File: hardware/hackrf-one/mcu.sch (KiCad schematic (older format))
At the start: 132 parts, among them J1 GSG-USB-MICRO-B, P1 1V8, P10 CTOUT_2, P11 CTIN_2, P12 U3_RXD, P13 U3_TXD, P19 SPIFI, P20 GPIO, P21 ANALOG, P22 I2S, P23 DBGEN, P24 TRST, P25 LPC_ISP, P26 LPC_JTAG, P27 CONN_3, P28 SD, P29 CPLD_JTAG, P3 GND, P30 BANK2_AUX, P31 BANK1_AUX, P32 CONN_3, P33 CONN_3, P34 CONN_3, P35 GCK0, P5 WAKEUP, P6 TRACECLK, P7 CTIN_4, P8 VCC, P9 CTOUT_4, U20 W25Q80BV, U21 TPS62410, U22 GSG-IP4220CZ6, U23 LPC43XXFBD144, U24 GSG-XC2C64A-7VQG100C, X2 MCU_XTAL

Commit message: removed boot headers, added reset and DFU pushbuttons
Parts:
- removed P27, P32, P33, P34: CONN_3, symbol CONN_3
- removed R40, R42, R43, R82: 10k, symbol R
- added SW1: DFU, symbol SW_PUSH
- added SW2: RESET, symbol SW_PUSH
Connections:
- wire segments 529 -> 590
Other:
- note added: "Default boot configuration is SPIFI.\nPress SW1 during reset to switch to\nUSB0 (DFU mode)."
- note removed: "Default boot configuration is SPIFI.\nInstall headers and jumpers (and\noptionally resistors) to reconfigure."
- moved on the sheet: R67, R68, R7, R93

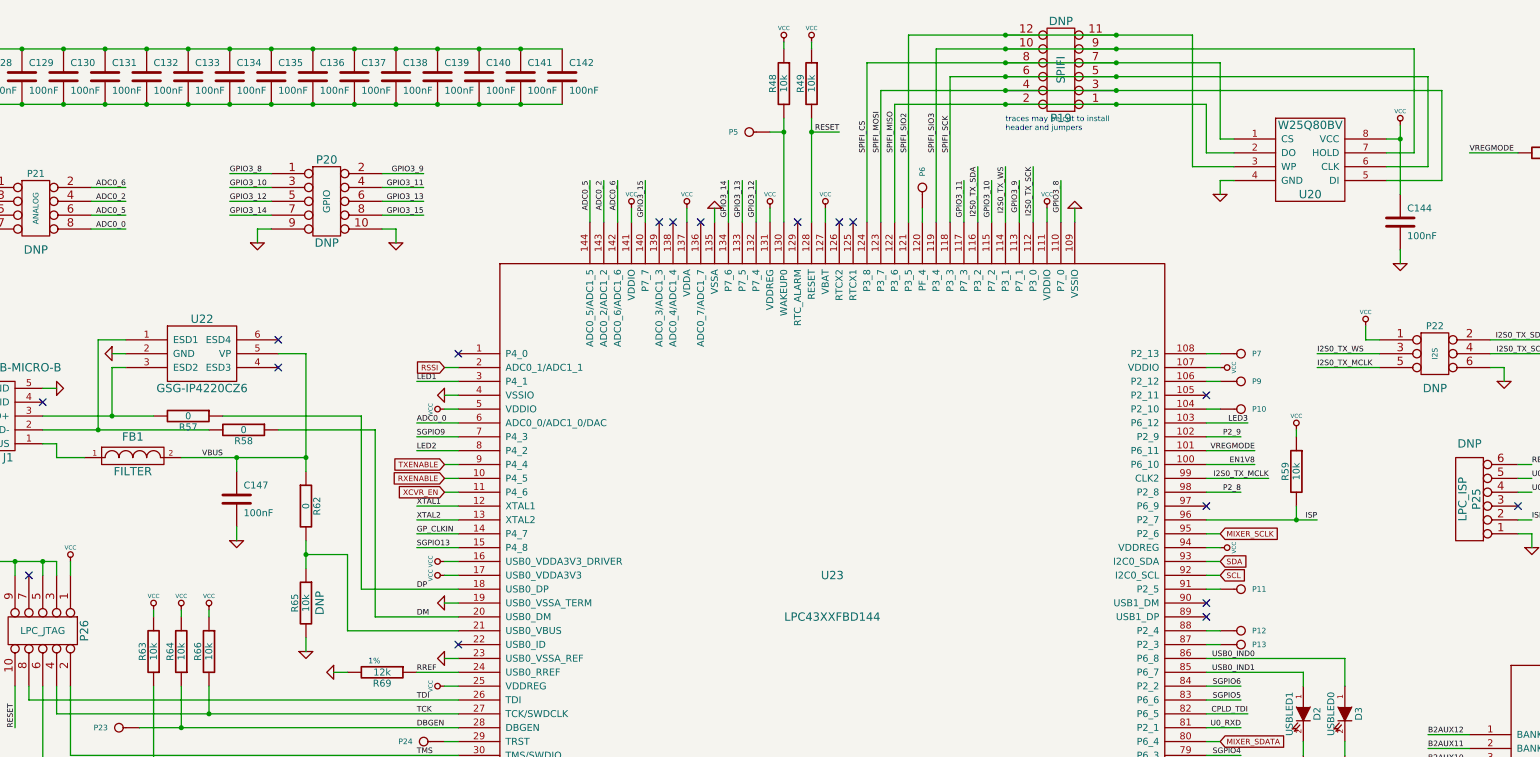
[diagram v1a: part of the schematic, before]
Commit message: removed some DNP parts and 0 ohm resistors
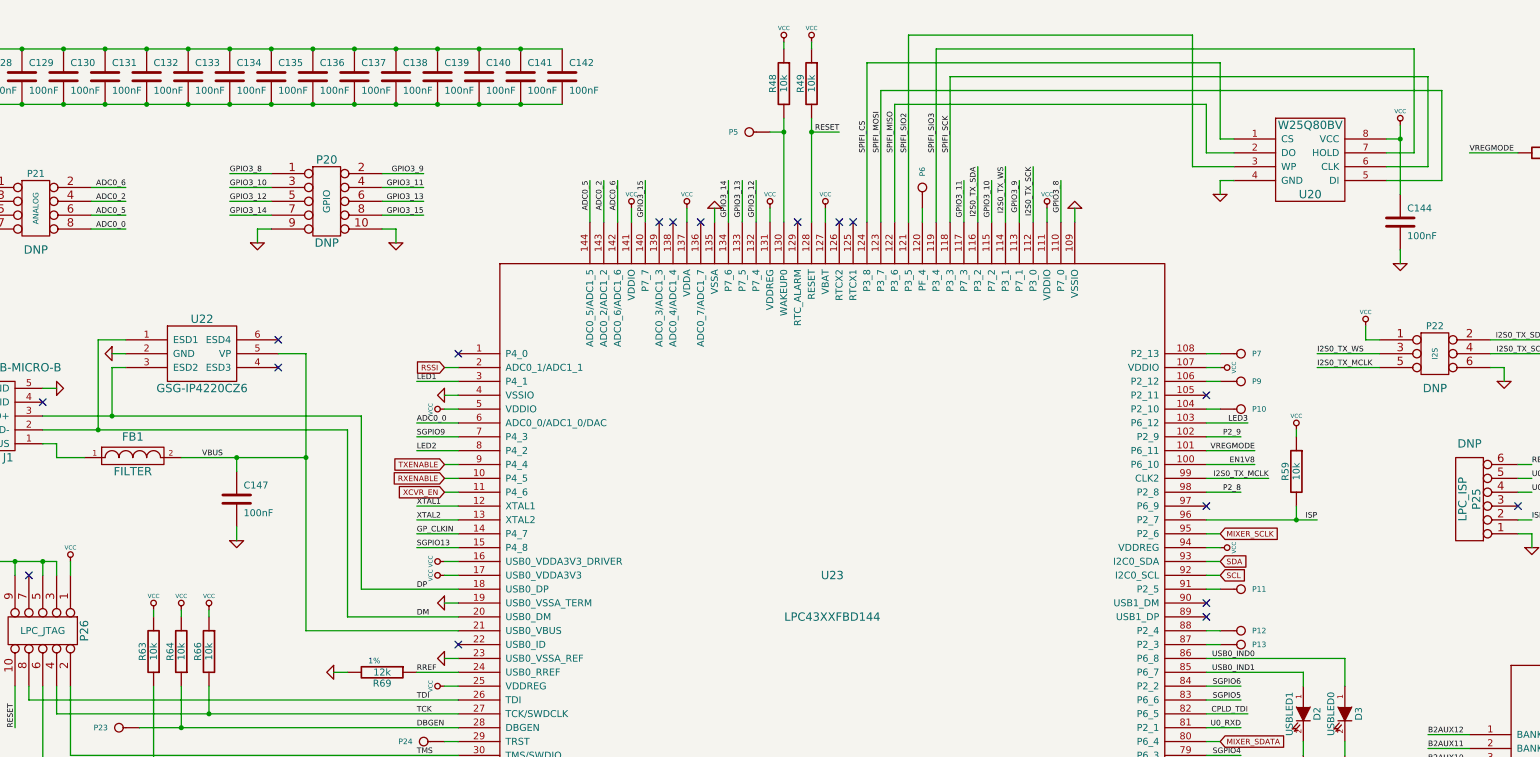
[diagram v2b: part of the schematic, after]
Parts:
- removed P19: SPIFI, symbol CONN_6X2
- removed R57, R58, R62: 0, symbol R
- removed R65: 10k, symbol R
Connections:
- net DM: now also J1.2 (D-), U22.1 (ESD1)
- net DP: now also J1.3 (D+), U22.3 (ESD2)
- net VBUS: now also U23.21 (USB0_VBUS)
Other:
- note removed: "traces may be cut to install\nheader and jumpers"
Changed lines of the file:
@@
 Wire Wire Line
 	11450 10000 11850 10000
-Connection ~ 8250 700
-Connection ~ 9050 700
 Wire Wire Line
-	7550 700  8250 700
+	7550 700  9600 700
 Wire Wire Line
-	8250 700  9050 700
-Wire Wire Line
-	9050 700  9600 700
-Connection ~ 8250 900
-Connection ~ 9050 900
-Wire Wire Line
-	7250 900  8250 900
-Wire Wire Line
-	8250 900  9050 900
-Wire Wire Line
-	9050 900  9800 900
-Connection ~ 8250 1100
-Connection ~ 9050 1100
-Wire Wire Line
-	7350 1100 8250 1100
-Wire Wire Line
-	8250 1100 9050 1100
-Wire Wire Line
-	9050 1100 11400 1100
+	7250 900  9800 900
 Wire Wire Line
 	12650 4400 12950 4400
@@
 	10400 5800 10400 5900
 Wire Wire Line
-	3000 3550 3700 3550
-Wire Wire Line
-	2600 3450 3600 3450
-Wire Wire Line
-	3200 4450 3500 4450
-Wire Wire Line
-	4300 3200 4000 3200
+	1300 3550 1700 3550
 Wire Wire Line
-	4300 5000 3500 5000
+	1700 3550 3500 3550
 Wire Wire Line
-	3500 5000 3500 4450
-Connection ~ 3200 4450
+	1300 3450 1800 3450
 Wire Wire Line
-	3200 4350 3200 4450
+	1800 3450 3600 3450
 Wire Wire Line
-	3200 4450 3200 4550
+	4300 3200 4000 3200
 Wire Wire Line
 	1900 7050 1900 7150
@@
 	1800 3000 1900 3000
 Wire Wire Line
-	3700 3550 3700 4900
+	3500 3550 3500 4900
 Connection ~ 750  2100
 Wire Wire Line
@@
 	5650 2050 5650 1750
 Wire Wire Line
-	3700 4900 4300 4900
+	3500 4900 4300 4900
 Wire Wire Line
 	2700 4350 2700 4250
@@
 	1600 7050 1600 7150
 Wire Wire Line
-	3200 5150 3200 5050
-Wire Wire Line
-	3200 3000 3200 3750
-Wire Wire Line
-	3200 3750 3200 3850
-Wire Wire Line
 	4300 3700 4000 3700
 Wire Wire Line
-	1300 3450 1800 3450
-Wire Wire Line
-	1800 3450 2100 3450
-Wire Wire Line
-	1300 3550 1700 3550
-Wire Wire Line
-	1700 3550 2500 3550
-Wire Wire Line
 	10400 5300 10400 5400
 Wire Wire Line
@@
 	5000 10250 5000 10150
 Wire Wire Line
-	7450 1200 8250 1200
-Wire Wire Line
-	8250 1200 9050 1200
-Wire Wire Line
-	9050 1200 9700 1200
-Connection ~ 9050 1200
-Connection ~ 8250 1200
-Wire Wire Line
-	7850 1000 8250 1000
-Wire Wire Line
-	8250 1000 9050 1000
+	7850 1000 11300 1000
 Wire Wire Line
-	9050 1000 11300 1000
-Connection ~ 9050 1000
-Connection ~ 8250 1000
-Wire Wire Line
-	7750 800  8250 800
-Wire Wire Line
-	8250 800  9050 800
-Wire Wire Line
-	9050 800  11200 800
-Connection ~ 9050 800
-Connection ~ 8250 800
+	7750 800  11200 800
 Wire Wire Line
 	10950 10000 10650 10000
@@
 C155 and C156 values\nare a guess. The datasheet\ndoesn't state the acceptable\nvoltage range for GP_CLKIN.
 $Comp
-L R R65
-U 1 1 506B55A7
-P 3200 4800
-F 0 "R65" V 3280 4800 50  0000 C CNN
-F 1 "10k" V 3200 4800 50  0000 C CNN
-F 2 "" H 3200 4800 60  0001 C CNN
-F 3 "" H 3200 4800 60  0001 C CNN
-F 4 "Stackpole" H 3200 4800 60  0001 C CNN "Manufacturer"
-F 5 "RMCF0402JT10K0" H 3200 4800 60  0001 C CNN "Part Number"
-F 6 "RES 10K OHM 1/16W 5% 0402 SMD" H 3200 4800 60  0001 C CNN "Description"
-F 7 "DNP" V 3100 4800 60  0000 C CNN "Note"
-	1    3200 4800
-	-1   0    0    -1
-$EndComp
-$Comp
-L R R62
-U 1 1 506B54E9
-P 3200 4100
-F 0 "R62" V 3280 4100 50  0000 C CNN
-F 1 "0" V 3200 4100 50  0000 C CNN
-F 2 "" H 3200 4100 60  0001 C CNN
-F 3 "" H 3200 4100 60  0001 C CNN
-F 4 "Stackpole" H 3200 4100 60  0001 C CNN "Manufacturer"
-F 5 "RMCF0402ZT0R00" H 3200 4100 60  0001 C CNN "Part Number"
-F 6 "RES 0.0 OHM 1/16W 0402 SMD" H 3200 4100 60  0001 C CNN "Description"
-	1    3200 4100
-	1    0    0    -1
-$EndComp
-$Comp
 L C C125
 U 1 1 505E9E4C
@@
 Text Notes 2200 9200 0    40   ~ 0
 Default boot configuration is SPIFI.\nPress SW1 during reset to switch to\nUSB0 (DFU mode).
-Text Notes 8250 1400 0    40   ~ 0
-traces may be cut to install\nheader and jumpers
 Text Notes 12000 9550 0    40   ~ 0
 R97 may be installed to connect SGPIO8 to the CPLD.\nBy default SGPIO8 is used as a clock input.
@@
 P2_8
 $Comp
-L R R58
-U 1 1 503F9D27
-P 2750 3550
-F 0 "R58" V 2830 3550 50  0000 C CNN
-F 1 "0" V 2750 3550 50  0000 C CNN
-F 2 "" H 2750 3550 60  0001 C CNN
-F 3 "" H 2750 3550 60  0001 C CNN
-F 4 "Stackpole" H 2750 3550 60  0001 C CNN "Manufacturer"
-F 5 "RMCF0402ZT0R00" H 2750 3550 60  0001 C CNN "Part Number"
-F 6 "RES 0.0 OHM 1/16W 0402 SMD" H 2750 3550 60  0001 C CNN "Description"
-	1    2750 3550
-	0    1    1    0
-$EndComp
-$Comp
-L R R57
-U 1 1 503F9D26
-P 2350 3450
-F 0 "R57" V 2430 3450 50  0000 C CNN
-F 1 "0" V 2350 3450 50  0000 C CNN
-F 2 "" H 2350 3450 60  0001 C CNN
-F 3 "" H 2350 3450 60  0001 C CNN
-F 4 "Stackpole" H 2350 3450 60  0001 C CNN "Manufacturer"
-F 5 "RMCF0402ZT0R00" H 2350 3450 60  0001 C CNN "Part Number"
-F 6 "RES 0.0 OHM 1/16W 0402 SMD" H 2350 3450 60  0001 C CNN "Description"
-	1    2350 3450
-	0    1    1    0
-$EndComp
-$Comp
 L R R59
 U 1 1 503F9A36
@@
 Text Label 4000 3200 0    40   ~ 0
 LED1
-$Comp
-L GND #PWR245
-U 1 1 4F83C49F
-P 3200 5150
-F 0 "#PWR245" H 3200 5150 30  0001 C CNN
-F 1 "GND" H 3200 5080 30  0001 C CNN
-F 2 "" H 3200 5150 60  0001 C CNN
-F 3 "" H 3200 5150 60  0001 C CNN
-	1    3200 5150
-	1    0    0    -1
-$EndComp
 Text Label 1300 6300 3    40   ~ 0
 LED3
@@
 $EndComp
 $Comp
-L CONN_6X2 P19
-U 1 1 4F825D84
-P 8650 950
-F 0 "P19" H 8650 1300 60  0000 C CNN
-F 1 "SPIFI" V 8650 950 60  0000 C CNN
-F 2 "" H 8650 950 60  0001 C CNN
-F 3 "" H 8650 950 60  0001 C CNN
-F 4 "DNP" H 8650 600 60  0000 C CNN "Note"
-	1    8650 950
-	-1   0    0    1
-$EndComp
-$Comp
 L W25Q80BV U20
 U 1 1 4F825D1B
@@
 Text Label 750  8600 0    40   ~ 0
 RESET
+Wire Wire Line
+	4300 5000 3200 5000
+Wire Wire Line
+	3200 5000 3200 3750
+Wire Wire Line
+	3200 3750 3200 3000
+Wire Wire Line
+	7350 1100 11400 1100
+Wire Wire Line
+	7450 1200 9700 1200
 $EndSCHEMATC

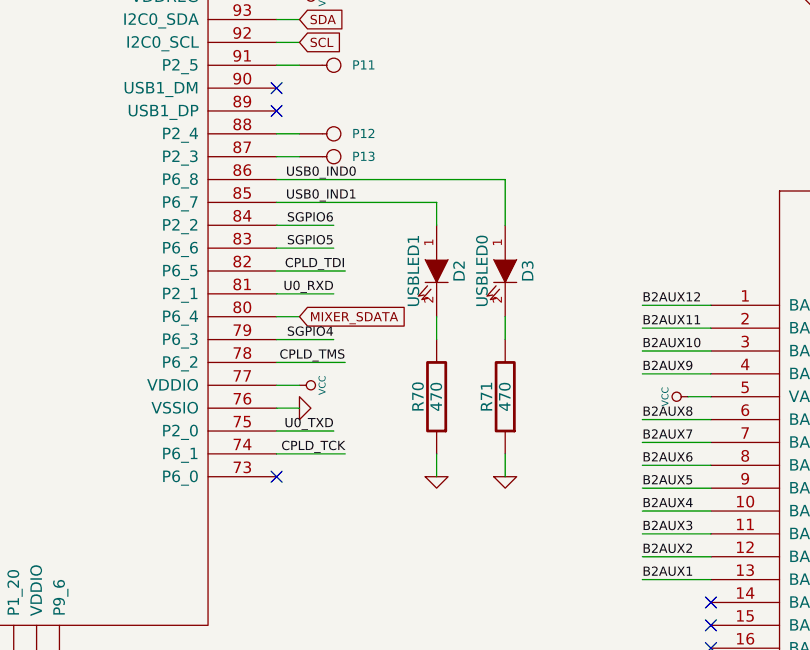
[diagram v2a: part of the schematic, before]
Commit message: removed USB LEDs
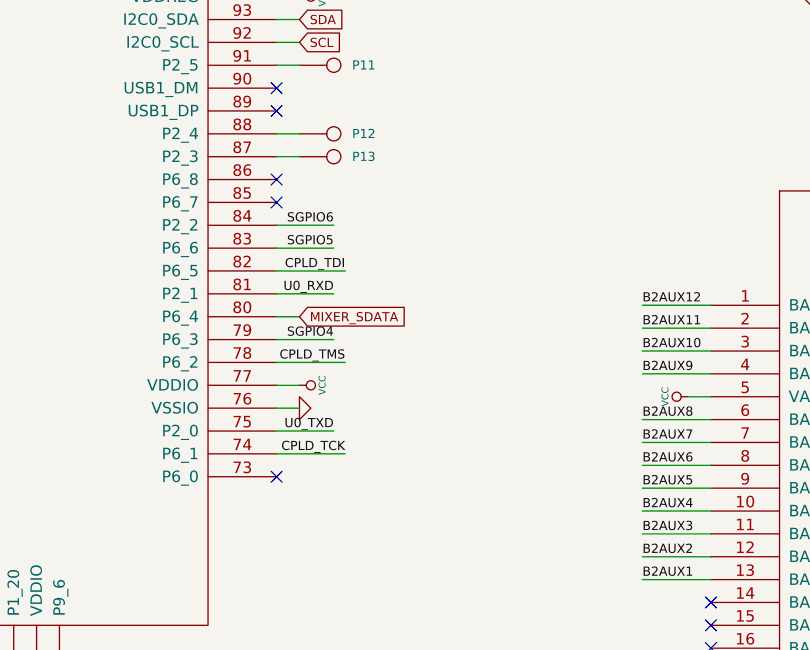
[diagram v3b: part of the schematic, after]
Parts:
- removed D2: USBLED1, symbol LED
- removed D3: USBLED0, symbol LED
- removed R70, R71: 470, symbol R
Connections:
- net USB0_IND0: no longer names the net of U23.86 (P6_8)
- net USB0_IND1: no longer names the net of U23.85 (P6_7)
- no-connect marks 27 -> 29
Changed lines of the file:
@@
 $EndDescr
 Wire Wire Line
-	9700 5300 10400 5300
-Wire Wire Line
 	9800 5800 9700 5800
 Wire Wire Line
@@
 	4300 4200 4000 4200
 Wire Wire Line
-	10400 5800 10400 5900
-Wire Wire Line
 	1300 3550 1700 3550
 Wire Wire Line
@@
 Wire Wire Line
 	8050 2050 8050 1650
-Wire Wire Line
-	10400 6400 10400 6500
 Connection ~ 1700 3550
 Wire Wire Line
@@
 	4300 3700 4000 3700
 Wire Wire Line
-	10400 5300 10400 5400
-Wire Wire Line
-	10700 5400 10700 5200
-Wire Wire Line
-	10700 6400 10700 6500
-Wire Wire Line
-	10700 5800 10700 5900
-Wire Wire Line
 	4300 4300 4000 4300
 Wire Wire Line
@@
 Wire Wire Line
 	9700 4300 9800 4300
-Wire Wire Line
-	10700 5200 9700 5200
 Text Notes 500  5200 0    40   ~ 0
 Cortex Debug\nConnector\n(10 pin 50 mil)
@@
 $EndComp
 $Comp
-L R R71
-U 1 1 503C51B5
-P 10700 6150
-F 0 "R71" V 10780 6150 50  0000 C CNN
-F 1 "470" V 10700 6150 50  0000 C CNN
-F 2 "" H 10700 6150 60  0001 C CNN
-F 3 "" H 10700 6150 60  0001 C CNN
-F 4 "Stackpole" H 10700 6150 60  0001 C CNN "Manufacturer"
-F 5 "RMCF0402JT470R" H 10700 6150 60  0001 C CNN "Part Number"
-F 6 "RES TF 1/16W 470 OHM 5% 0402" H 10700 6150 60  0001 C CNN "Description"
-	1    10700 6150
-	-1   0    0    1
-$EndComp
-$Comp
-L R R70
-U 1 1 503C51AC
-P 10400 6150
-F 0 "R70" V 10480 6150 50  0000 C CNN
-F 1 "470" V 10400 6150 50  0000 C CNN
-F 2 "" H 10400 6150 60  0001 C CNN
-F 3 "" H 10400 6150 60  0001 C CNN
-F 4 "Stackpole" H 10400 6150 60  0001 C CNN "Manufacturer"
-F 5 "RMCF0402JT470R" H 10400 6150 60  0001 C CNN "Part Number"
-F 6 "RES TF 1/16W 470 OHM 5% 0402" H 10400 6150 60  0001 C CNN "Description"
-	1    10400 6150
-	-1   0    0    1
-$EndComp
-$Comp
 L R R76
 U 1 1 503C51AA
@@
 Text Label 4000 4300 0    40   ~ 0
 GP_CLKIN
-Text Label 10050 5300 2    40   ~ 0
-USB0_IND1
-$Comp
-L LED D3
-U 1 1 4F87ACCD
-P 10700 5600
-F 0 "D3" H 10700 5700 50  0000 C CNN
-F 1 "USBLED0" H 10700 5500 50  0000 C CNN
-F 2 "" H 10700 5600 60  0001 C CNN
-F 3 "" H 10700 5600 60  0001 C CNN
-F 4 "Everlight" H 10700 5600 60  0001 C CNN "Manufacturer"
-F 5 "QTLP600CYTR" H 10700 5600 60  0001 C CNN "Part Number"
-F 6 "LED YLW SUPER BRIGHT 0606 SMD" H 10700 5600 60  0001 C CNN "Description"
-	1    10700 5600
-	0    1    1    0
-$EndComp
-$Comp
-L GND #PWR256
-U 1 1 4F87ACCB
-P 10700 6500
-F 0 "#PWR256" H 10700 6500 30  0001 C CNN
-F 1 "GND" H 10700 6430 30  0001 C CNN
-F 2 "" H 10700 6500 60  0001 C CNN
-F 3 "" H 10700 6500 60  0001 C CNN
-	1    10700 6500
-	1    0    0    -1
-$EndComp
 $Comp
 L LPC43XXFBD144 U23
@@
 	1    0    0    -1
 $EndComp
-Text Label 10050 5200 2    40   ~ 0
-USB0_IND0
 Text Label 10000 3500 2    40   ~ 0
 LED3
@@
 Text Label 8250 1650 3    40   ~ 0
 I2S0_TX_WS
-$Comp
-L GND #PWR255
-U 1 1 4F83B36A
-P 10400 6500
-F 0 "#PWR255" H 10400 6500 30  0001 C CNN
-F 1 "GND" H 10400 6430 30  0001 C CNN
-F 2 "" H 10400 6500 60  0001 C CNN
-F 3 "" H 10400 6500 60  0001 C CNN
-	1    10400 6500
-	1    0    0    -1
-$EndComp
-$Comp
-L LED D2
-U 1 1 4F83B14A
-P 10400 5600
-F 0 "D2" H 10400 5700 50  0000 C CNN
-F 1 "USBLED1" H 10400 5500 50  0000 C CNN
-F 2 "" H 10400 5600 60  0001 C CNN
-F 3 "" H 10400 5600 60  0001 C CNN
-F 4 "Everlight" H 10400 5600 60  0001 C CNN "Manufacturer"
-F 5 "QTLP601C4TR" H 10400 5600 60  0001 C CNN "Part Number"
-F 6 "LED GREEN STD BRIGHT 0603 SMD" H 10400 5600 60  0001 C CNN "Description"
-	1    10400 5600
-	0    1    1    0
-$EndComp
 NoConn ~ 3000 2900
 $Comp
@@
 Wire Wire Line
 	7450 1200 9700 1200
+NoConn ~ 9700 5200
+NoConn ~ 9700 5300
 $EndSCHEMATC

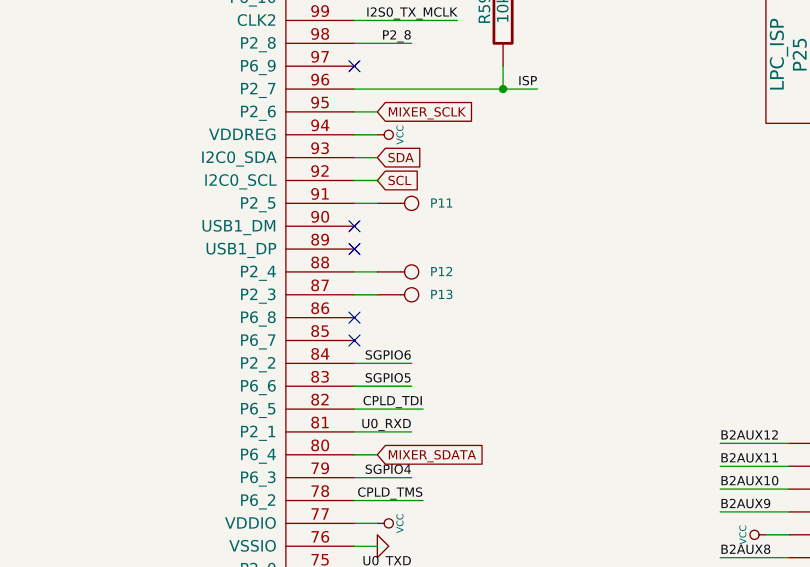
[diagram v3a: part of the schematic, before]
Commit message: removed U3 test points (there is another UART exposed on the ISP header)
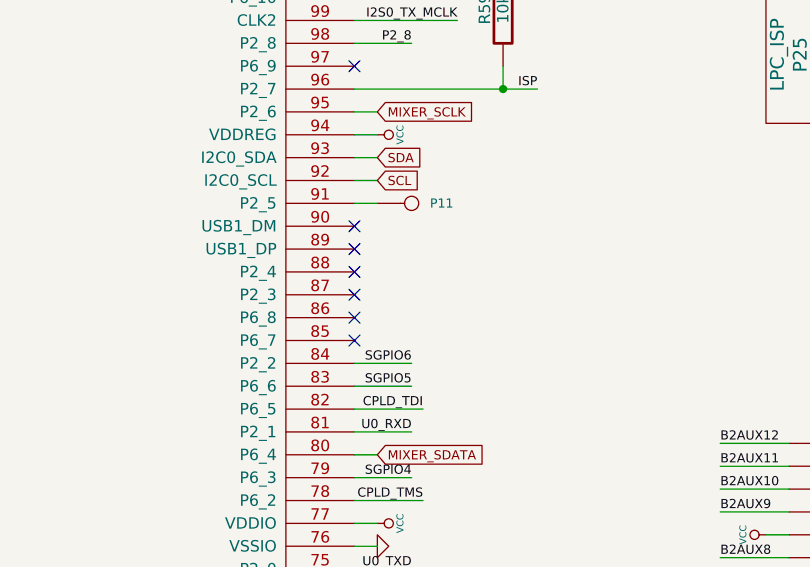
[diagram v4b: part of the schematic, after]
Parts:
- removed P12: U3_RXD, symbol CONN_1
- removed P13: U3_TXD, symbol CONN_1
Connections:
- no-connect marks 29 -> 31
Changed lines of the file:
@@
 	9700 4000 9950 4000
 Wire Wire Line
-	9700 5000 9800 5000
-Wire Wire Line
 	2300 4850 2300 4900
 Wire Wire Line
@@
 	2100 4850 2100 4900
 Wire Wire Line
-	9700 5100 9800 5100
-Wire Wire Line
 	9700 3600 9950 3600
 Wire Wire Line
@@
 $EndComp
 $Comp
-L CONN_1 P13
-U 1 1 50457304
-P 9950 5100
-F 0 "P13" H 10030 5100 40  0000 L CNN
-F 1 "U3_TXD" H 9950 5155 30  0001 C CNN
-F 2 "" H 9950 5100 60  0001 C CNN
-F 3 "" H 9950 5100 60  0001 C CNN
-F 4 "DNP" H 9950 5100 60  0001 C CNN "Note"
-	1    9950 5100
-	1    0    0    -1
-$EndComp
-$Comp
-L CONN_1 P12
-U 1 1 504572EF
-P 9950 5000
-F 0 "P12" H 10030 5000 40  0000 L CNN
-F 1 "U3_RXD" H 9950 5055 30  0001 C CNN
-F 2 "" H 9950 5000 60  0001 C CNN
-F 3 "" H 9950 5000 60  0001 C CNN
-F 4 "DNP" H 9950 5000 60  0001 C CNN "Note"
-	1    9950 5000
-	1    0    0    -1
-$EndComp
-$Comp
 L CONN_8X2 P30
 U 1 1 504571A2
@@
 NoConn ~ 9700 5200
 NoConn ~ 9700 5300
+NoConn ~ 9700 5100
+NoConn ~ 9700 5000
 $EndSCHEMATC

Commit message: fixed VCCIO1 to VCC
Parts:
- removed R60: 0, symbol R-SHORTED
- removed R61: 0, symbol R
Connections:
- net VCCIO1 is gone; now on net VCC: C153.1, C154.1, U24.38 (VCCIO1), U24.51 (VCCIO1)
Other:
- note removed: "bank 1 power selection"
- moved on the sheet: C148, C149, C150, C153, C154

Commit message: regulator feedback fix
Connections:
- net REG_OUT1: now also U21.4 (FB1)
- net VCC: no longer U21.4 (FB1)
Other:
- moved on the sheet: C143
